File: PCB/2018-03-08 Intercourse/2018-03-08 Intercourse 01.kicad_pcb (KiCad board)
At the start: 2 copper layers, 85.6 x 54 mm, 50 parts, among them J1 USB_C_Receptacle, J2 TP_RST, J3 TP_TX, J4 TP_RX, J5 TP_GPIO0, J6 TP_GND1, J7 TP_GND2, J8 TP_GND3, U1 LTC3225, U2 TPS61221DCKR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

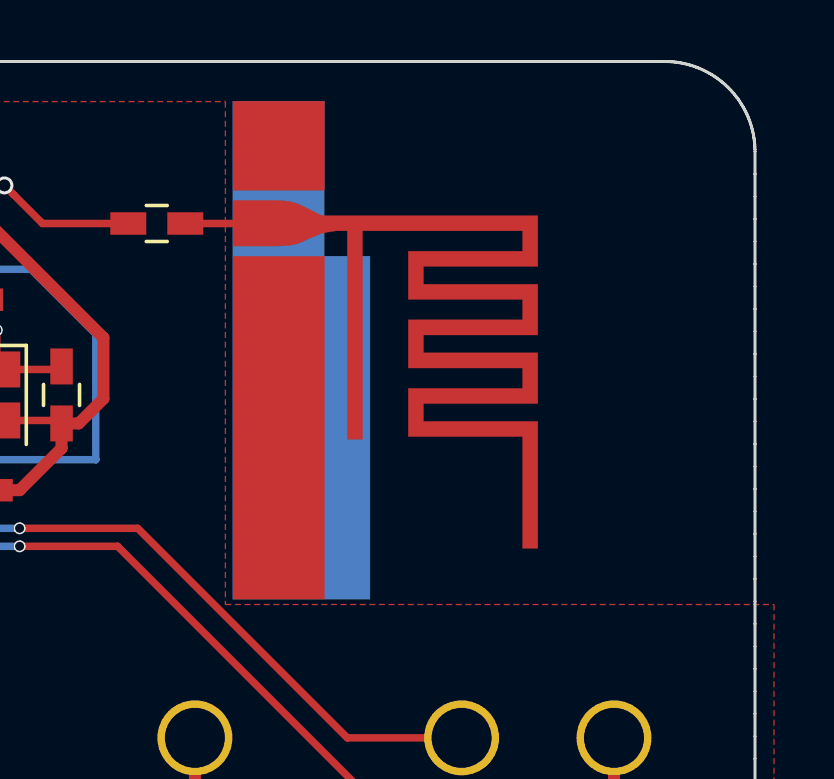
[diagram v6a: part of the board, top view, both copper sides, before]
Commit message: updated antenna design
board ready for revision
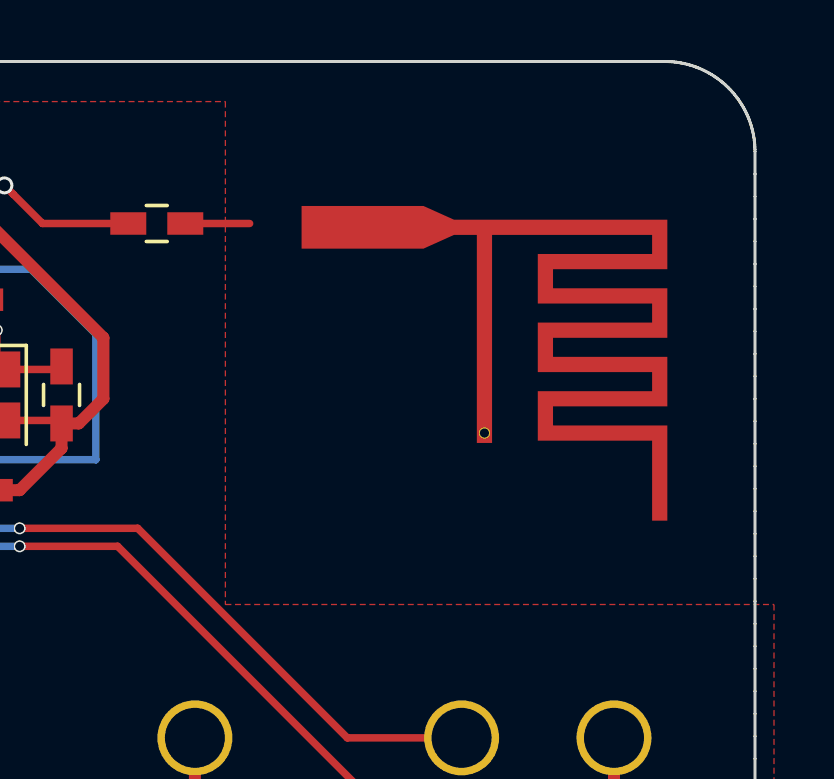
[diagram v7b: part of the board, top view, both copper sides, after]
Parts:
- AE1: value Antenna -> Antenna_Dipole; footprint MyAntennas:AN91445 -> MyAntennas:AN91445_47_mils
- moved AE1 4.17 mm to (182.1, 80.1)
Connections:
- AE1 pad 1: Net-(AE1-Pad1) -> GND
- AE1 pad 2: (no net) -> Net-(AE1-Pad2)
- C10 pad 1: Net-(AE1-Pad1) -> Net-(AE1-Pad2)
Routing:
- net Net-(AE1-Pad2): track 0.00 -> 2.14 mm
- net Net-(AE1-Pad1): track 2.14 -> 0.00 mm

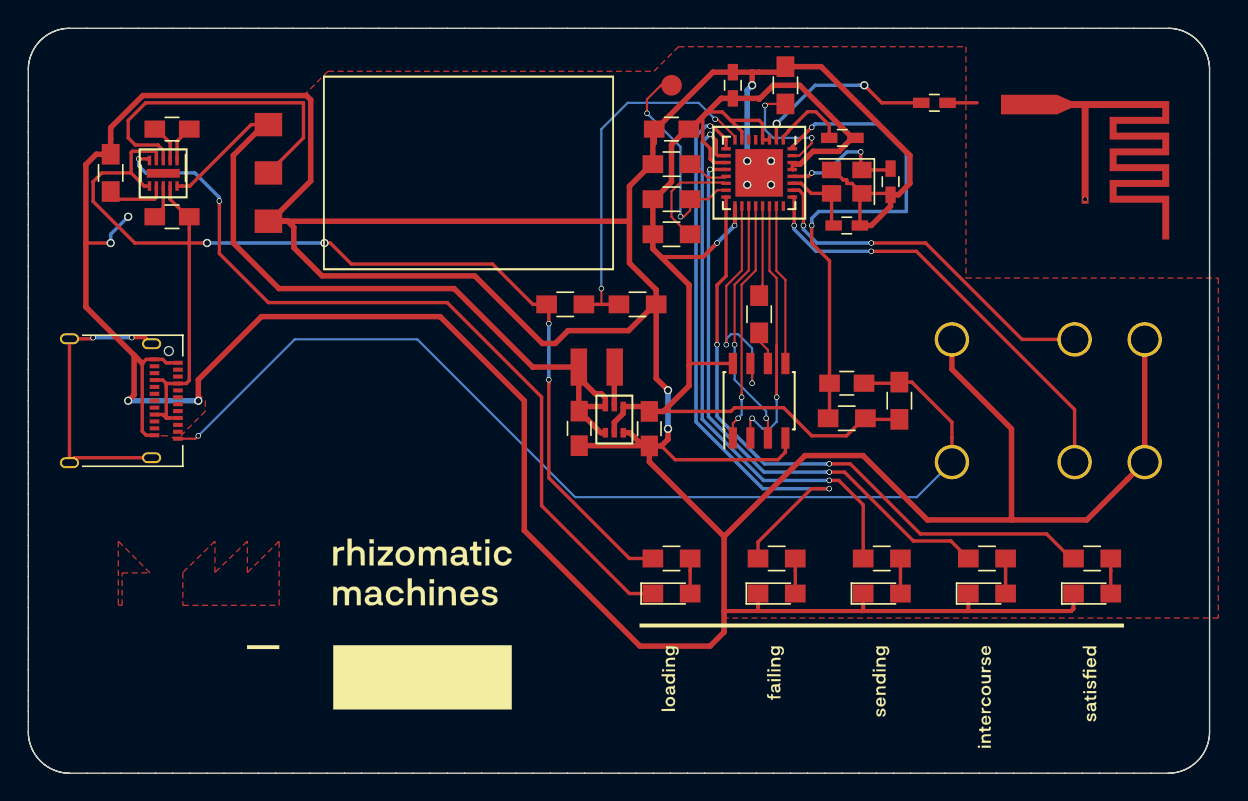
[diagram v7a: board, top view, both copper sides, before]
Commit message: updated antenna design
- had to move components also
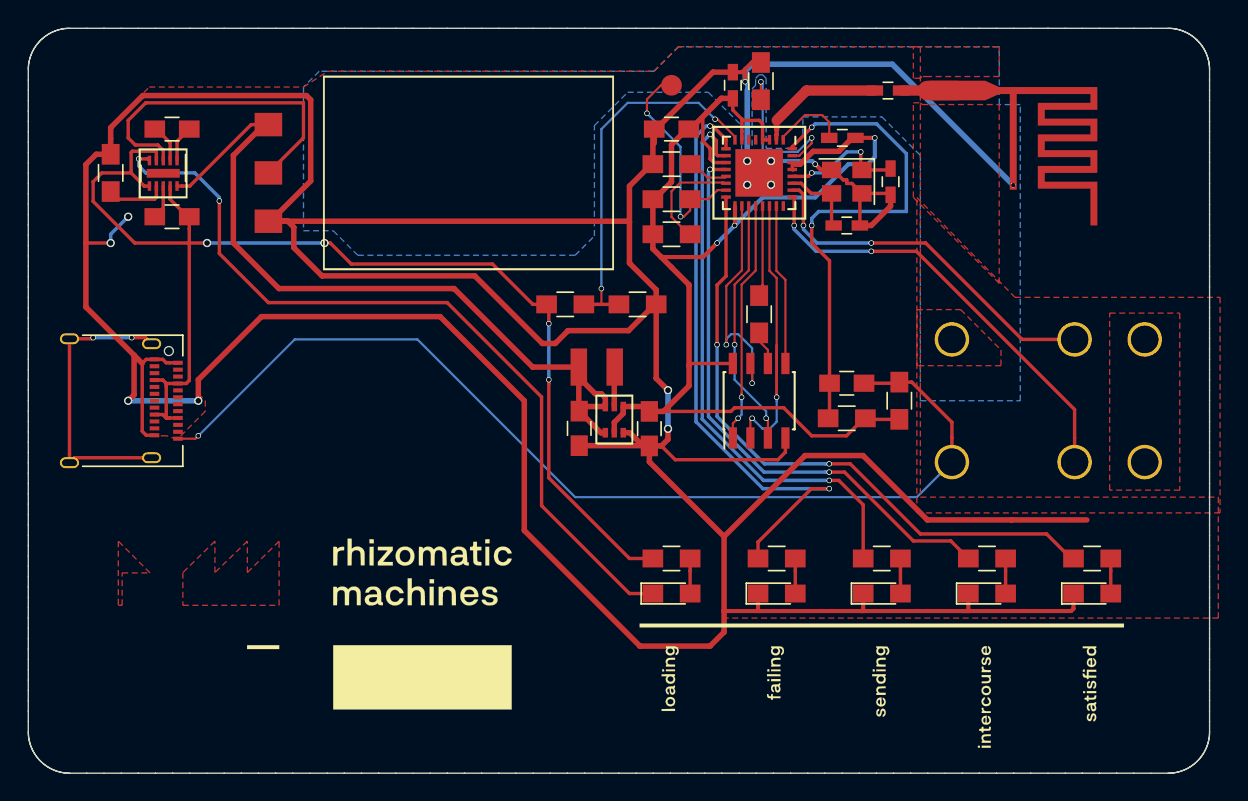
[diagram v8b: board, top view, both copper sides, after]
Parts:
- moved AE1 5.31 mm to (176.9, 79.1)
- moved C10 3.48 mm to (171.9, 79.1)
- moved R6 1.80 mm to (162.7, 78.4)
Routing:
- net GND: track 399.4 -> 381.5 mm, vias 11 -> 12
- net Net-(R6-Pad2): track 9.09 -> 12.6 mm
- net VDD: track 91.8 -> 95.0 mm, vias 2 -> 3
- net Net-(C10-Pad2): track 13.4 -> 10.4 mm, vias 2 -> 0
- net Net-(AE1-Pad2): track 2.14 -> 4.06 mm
- added copper zone on B.Cu, net GND
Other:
- net class Null added: clearance 0, trace_width 0.25, via_dia 0.6, via_drill 0.4
